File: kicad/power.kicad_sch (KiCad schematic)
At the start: 27 parts, among them J28 Eurorack Power Small, J29 Conn_01x04_Socket, J30 Conn_01x04_Header, U1 CD4093, U2 TL072, U3 TL072, U4 TL074, U5 LM13700, U6 LM13700, U7 LM13700

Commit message: Tweaking schematic and bom values
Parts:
- C21, C22: value 1uF -> 10uF
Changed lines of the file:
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@@
   (symbol (lib_id "Device:C_Polarized") (at 67.31 68.58 0) (unit 1)
     (in_bom yes) (on_board yes) (fields_autoplaced)
-    (property "Reference" "C22" (id 0) (at 70.231 66.7825 0)
-      (effects (font (size 1.27 1.27)) (justify left))
-    )
-    (property "Value" "1uF" (id 1) (at 70.231 69.5576 0)
+    (property "Reference" "C22" (id 0) (at 70.231 66.8563 0)
+      (effects (font (size 1.27 1.27)) (justify left))
+    )
+    (property "Value" "10uF" (id 1) (at 70.231 69.3932 0)
       (effects (font (size 1.27 1.27)) (justify left))
     )
@@
   (symbol (lib_id "Device:C_Polarized") (at 67.31 49.53 0) (unit 1)
     (in_bom yes) (on_board yes) (fields_autoplaced)
-    (property "Reference" "C21" (id 0) (at 70.231 47.7325 0)
-      (effects (font (size 1.27 1.27)) (justify left))
-    )
-    (property "Value" "1uF" (id 1) (at 70.231 50.5076 0)
-      (effects (font (size 1.27 1.27)) (justify left))
-    )
+    (property "Reference" "C21" (id 0) (at 70.231 47.8063 0)
+      (effects (font (size 1.27 1.27)) (justify left))
+    )
+    (property "Value" "10uF" (id 1) (at 70.231 50.3432 0)
+      (effects (font (size 1.27 1.27)) (justify left))
+    )

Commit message: Moving mixer opamp to front board
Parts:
- removed U3: TL072, rumblesan-standard-parts:DIP-8_W7.62mm_Socket, symbol Amplifier_Operational:TL072
- added U3: TL074, rumblesan-standard-parts:DIP-14_W7.62mm_Socket, symbol Amplifier_Operational:TL074
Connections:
- net +12V: now also U3.4 (V+)
- net -12V: now also U3.11 (V-)
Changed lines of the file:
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@@
     (pin "2")
   )
-  (symbol (lib_id "Amplifier_Operational:TL072") (at 111.76 46.99 0) (unit 3)
+  (symbol (lib_id "Amplifier_Operational:TL074") (at 111.76 46.99 0) (unit 5)
     (in_bom yes) (on_board yes) (fields_autoplaced)
-    (property "Reference" "U3" (id 0) (at 109.855 46.0815 0)
+    (property "Reference" "U3" (id 0) (at 109.855 46.1553 0)
       (effects (font (size 1.27 1.27)) (justify left))
     )
-    (property "Value" "TL072" (id 1) (at 109.855 48.8566 0)
+    (property "Value" "TL074" (id 1) (at 109.855 48.6922 0)
       (effects (font (size 1.27 1.27)) (justify left))
     )
-    (property "Footprint" "rumblesan-standard-parts:DIP-8_W7.62mm_Socket" (id 2) (at 111.76 46.99 0)
+    (property "Footprint" "rumblesan-standard-parts:DIP-14_W7.62mm_Socket" (id 2) (at 110.49 44.45 0)
       (effects (font (size 1.27 1.27)) hide)
     )
-    (property "Datasheet" "http://www.ti.com/lit/ds/symlink/tl071.pdf" (id 3) (at 111.76 46.99 0)
+    (property "Datasheet" "http://www.ti.com/lit/ds/symlink/tl071.pdf" (id 3) (at 113.03 41.91 0)
       (effects (font (size 1.27 1.27)) hide)
     )
@@
     (pin "6")
     (pin "7")
+    (pin "10")
+    (pin "8")
+    (pin "9")
+    (pin "12")
+    (pin "13")
+    (pin "14")
+    (pin "11")
     (pin "4")
-    (pin "8")
   )
   (symbol (lib_id "power:GND") (at 153.67 78.74 0) (unit 1)

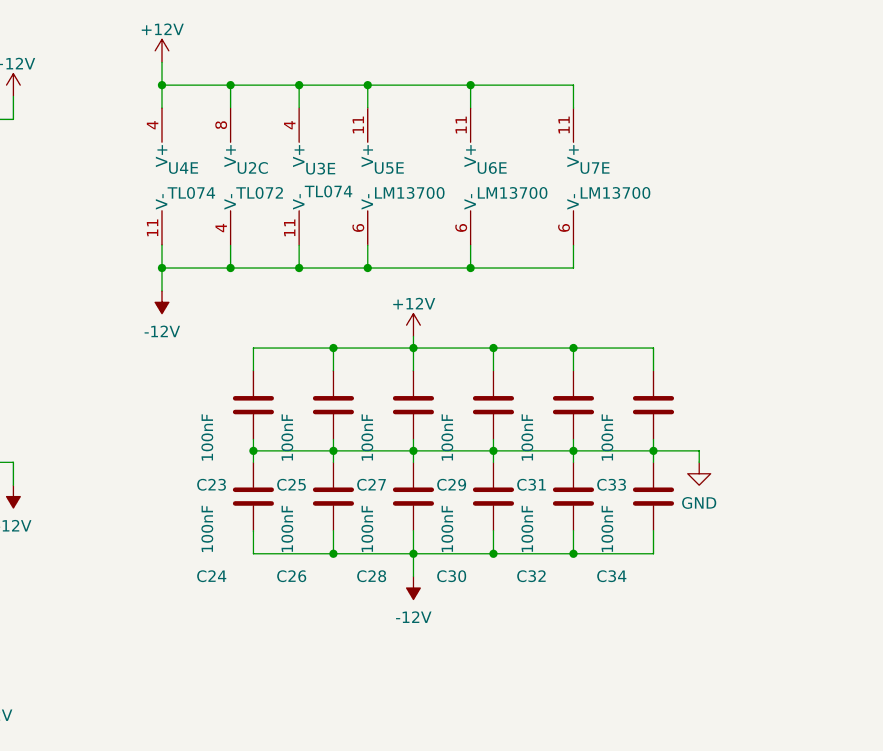
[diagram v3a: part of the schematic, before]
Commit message: slimlining opamp count and more moving around
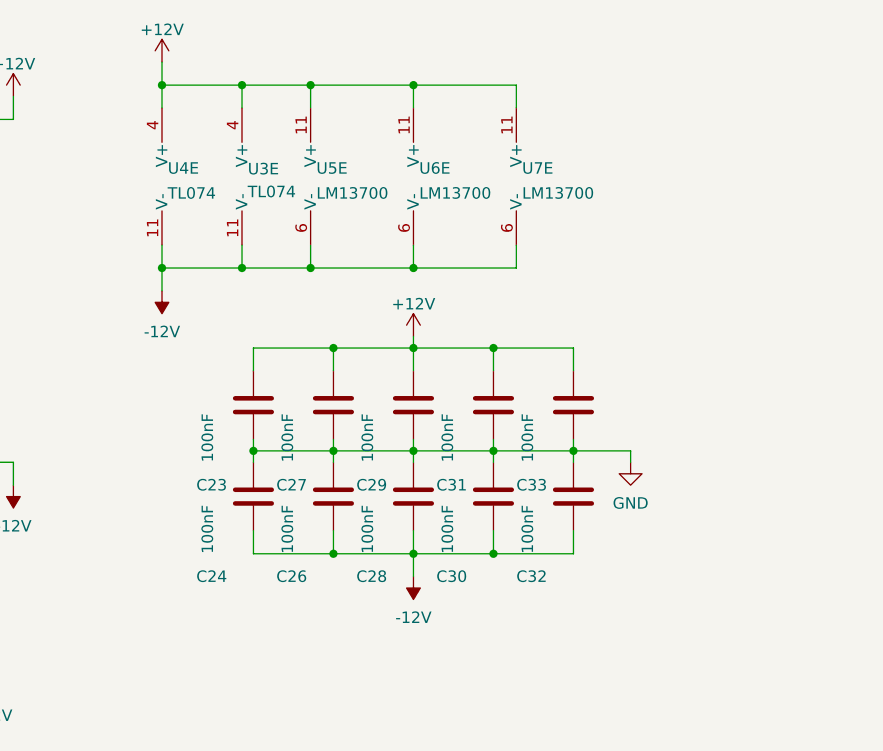
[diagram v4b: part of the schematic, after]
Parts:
- removed C25, C34: 100nF, rumblesan-standard-parts:C_Rect_L7.0mm_W3.5mm_P5.00mm, symbol Device:C
- removed U2: TL072, rumblesan-standard-parts:DIP-8_W7.62mm_Socket, symbol Amplifier_Operational:TL072
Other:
- moved on the sheet: C27, C29, C31, C33, U3E, U5E, U6E, U7E

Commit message: Final fixes and tweaks (hopefully)
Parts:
- added C25, C34: 100nF, rumblesan-standard-parts:C_Rect_L7.0mm_W3.5mm_P5.00mm, symbol Device:C
- added U2: TL072, rumblesan-standard-parts:DIP-8_W7.62mm_Socket, symbol Amplifier_Operational:TL072
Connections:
- net +12V: now also C25.1, U2.8 (V+)
- net -12V: now also C34.2, U2.4 (V-)
- net GND: now also C25.2, C34.1
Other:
- moved on the sheet: C32, C33, U3E, U4E, U5E, U6E, U7E

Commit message: geographically reannotate all the parts
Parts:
- renumbered C21 to C10, C34 to C13, C22 to C14, C23 to C22, C28 to C25, C29 to C26, C32 to C28, C33 to C31, C24 to C32, C26 to C34, C31 to C4, C30 to C5, C27 to C8, C25 to C9, D7 to D3, D8 to D4, J29 to J2, J28 to J3, J30 to J6, U3 to U1, U1 to U2, U2 to U3, U5 to U4, U4 to U5, U7 to U6, U6 to U7
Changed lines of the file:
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@@
   (symbol (lib_id "Device:C") (at 139.7 72.39 0) (unit 1)
     (in_bom yes) (on_board yes)
-    (property "Reference" "C25" (id 0) (at 133.35 81.28 0)
+    (property "Reference" "C9" (id 0) (at 133.35 81.28 0)
       (effects (font (size 1.27 1.27)) (justify left))
     )
@@
   (symbol (lib_id "Device:C_Polarized") (at 67.31 68.58 0) (unit 1)
     (in_bom yes) (on_board yes) (fields_autoplaced)
-    (property "Reference" "C22" (id 0) (at 70.231 66.8563 0)
+    (property "Reference" "C14" (id 0) (at 70.231 66.8563 0)
       (effects (font (size 1.27 1.27)) (justify left))
     )
@@
   (symbol (lib_id "Device:C") (at 139.7 82.55 0) (unit 1)
     (in_bom yes) (on_board yes)
-    (property "Reference" "C34" (id 0) (at 133.35 91.44 0)
+    (property "Reference" "C13" (id 0) (at 133.35 91.44 0)
       (effects (font (size 1.27 1.27)) (justify left))
     )
@@
   (symbol (lib_id "Device:C") (at 113.03 72.39 0) (unit 1)
     (in_bom yes) (on_board yes)
-    (property "Reference" "C27" (id 0) (at 106.68 81.28 0)
+    (property "Reference" "C8" (id 0) (at 106.68 81.28 0)
       (effects (font (size 1.27 1.27)) (justify left))
     )
@@
   (symbol (lib_id "Amplifier_Operational:TL074") (at 119.38 36.83 0) (unit 5)
     (in_bom yes) (on_board yes) (fields_autoplaced)
-    (property "Reference" "U3" (id 0) (at 117.475 35.9953 0)
+    (property "Reference" "U1" (id 0) (at 117.475 35.9953 0)
       (effects (font (size 1.27 1.27)) (justify left))
     )
@@
   (symbol (lib_id "Device:D") (at 60.96 78.74 0) (unit 1)
     (in_bom yes) (on_board yes) (fields_autoplaced)
-    (property "Reference" "D8" (id 0) (at 60.96 73.5035 0))
+    (property "Reference" "D4" (id 0) (at 60.96 73.5035 0))
     (property "Value" "1N5818" (id 1) (at 60.96 76.2786 0))
     (property "Footprint" "rumblesan-standard-parts:D_DO-41_SOD81_P10.16mm_Horizontal" (id 2) (at 60.96 78.74 0)
@@
   (symbol (lib_id "Eurorack_Hardware:Eurorack Power Small") (at 46.99 59.69 0) (unit 1)
     (in_bom yes) (on_board yes)
-    (property "Reference" "J28" (id 0) (at 47.625 50.0593 0))
+    (property "Reference" "J3" (id 0) (at 47.625 50.0593 0))
     (property "Value" "Eurorack Power Small" (id 1) (at 43.18 59.69 90))
     (property "Footprint" "eurorack-power:Eurorack_PowerHeader_2x05_P2.54mm_Shrouded" (id 2) (at 46.99 68.58 0)
@@
   (symbol (lib_id "Connector:Conn_01x04_Female") (at 62.23 114.3 0) (unit 1)
     (in_bom yes) (on_board yes)
-    (property "Reference" "J29" (id 0) (at 58.42 109.22 0)
+    (property "Reference" "J2" (id 0) (at 58.42 109.22 0)
       (effects (font (size 1.27 1.27)) (justify left))
     )
@@
   (symbol (lib_id "Amplifier_Operational:LM13700") (at 149.86 36.83 0) (unit 5)
     (in_bom yes) (on_board yes)
-    (property "Reference" "U7" (id 0) (at 147.955 35.9215 0)
+    (property "Reference" "U6" (id 0) (at 147.955 35.9215 0)
       (effects (font (size 1.27 1.27)) (justify left))
     )
@@
   (symbol (lib_id "Device:C") (at 148.59 82.55 0) (unit 1)
     (in_bom yes) (on_board yes)
-    (property "Reference" "C32" (id 0) (at 142.24 91.44 0)
+    (property "Reference" "C28" (id 0) (at 142.24 91.44 0)
       (effects (font (size 1.27 1.27)) (justify left))
     )
@@
   (symbol (lib_id "Device:C_Polarized") (at 67.31 49.53 0) (unit 1)
     (in_bom yes) (on_board yes) (fields_autoplaced)
-    (property "Reference" "C21" (id 0) (at 70.231 47.8063 0)
+    (property "Reference" "C10" (id 0) (at 70.231 47.8063 0)
       (effects (font (size 1.27 1.27)) (justify left))
     )
@@
   (symbol (lib_id "Amplifier_Operational:TL072") (at 101.6 36.83 0) (unit 3)
     (in_bom yes) (on_board yes) (fields_autoplaced)
-    (property "Reference" "U2" (id 0) (at 99.695 35.9953 0)
+    (property "Reference" "U3" (id 0) (at 99.695 35.9953 0)
       (effects (font (size 1.27 1.27)) (justify left))
     )
@@
   (symbol (lib_id "Device:D") (at 60.96 40.64 180) (unit 1)
     (in_bom yes) (on_board yes) (fields_autoplaced)
-    (property "Reference" "D7" (id 0) (at 60.96 35.4035 0))
+    (property "Reference" "D3" (id 0) (at 60.96 35.4035 0))
     (property "Value" "1N5818" (id 1) (at 60.96 38.1786 0))
     (property "Footprint" "rumblesan-standard-parts:D_DO-41_SOD81_P10.16mm_Horizontal" (id 2) (at 60.96 40.64 0)
@@
   (symbol (lib_id "Device:C") (at 113.03 82.55 0) (unit 1)
     (in_bom yes) (on_board yes)
-    (property "Reference" "C26" (id 0) (at 106.68 91.44 0)
+    (property "Reference" "C34" (id 0) (at 106.68 91.44 0)
       (effects (font (size 1.27 1.27)) (justify left))
     )
@@
   (symbol (lib_id "Device:C") (at 130.81 72.39 0) (unit 1)
     (in_bom yes) (on_board yes)
-    (property "Reference" "C31" (id 0) (at 124.46 81.28 0)
+    (property "Reference" "C4" (id 0) (at 124.46 81.28 0)
       (effects (font (size 1.27 1.27)) (justify left))
     )
@@
   (symbol (lib_id "4xxx:HEF4093B") (at 199.39 57.15 0) (unit 5)
     (in_bom yes) (on_board yes)
-    (property "Reference" "U1" (id 0) (at 205.232 56.2415 0)
+    (property "Reference" "U2" (id 0) (at 205.232 56.2415 0)
       (effects (font (size 1.27 1.27)) (justify left))
     )
@@
   (symbol (lib_id "Device:C") (at 121.92 72.39 0) (unit 1)
     (in_bom yes) (on_board yes)
-    (property "Reference" "C29" (id 0) (at 115.57 81.28 0)
+    (property "Reference" "C26" (id 0) (at 115.57 81.28 0)
       (effects (font (size 1.27 1.27)) (justify left))
     )
@@
   (symbol (lib_id "Amplifier_Operational:LM13700") (at 138.43 36.83 0) (unit 5)
     (in_bom yes) (on_board yes) (fields_autoplaced)
-    (property "Reference" "U6" (id 0) (at 136.525 35.9215 0)
+    (property "Reference" "U7" (id 0) (at 136.525 35.9215 0)
       (effects (font (size 1.27 1.27)) (justify left))
     )
@@
   (symbol (lib_id "Device:C") (at 121.92 82.55 0) (unit 1)
     (in_bom yes) (on_board yes)
-    (property "Reference" "C28" (id 0) (at 115.57 91.44 0)
+    (property "Reference" "C25" (id 0) (at 115.57 91.44 0)
       (effects (font (size 1.27 1.27)) (justify left))
     )
@@
   (symbol (lib_id "Device:C") (at 148.59 72.39 0) (unit 1)
     (in_bom yes) (on_board yes)
-    (property "Reference" "C33" (id 0) (at 142.24 81.28 0)
+    (property "Reference" "C31" (id 0) (at 142.24 81.28 0)
       (effects (font (size 1.27 1.27)) (justify left))
     )
@@
   (symbol (lib_id "Connector:Conn_01x04_Male") (at 68.58 114.3 0) (unit 1)
     (in_bom yes) (on_board yes)
-    (property "Reference" "J30" (id 0) (at 71.12 109.22 0))
+    (property "Reference" "J6" (id 0) (at 71.12 109.22 0))
     (property "Value" "Conn_01x04_Header" (id 1) (at 67.31 115.57 90)
       (effects (font (size 1.27 1.27)) hide)
@@
   (symbol (lib_id "Amplifier_Operational:TL074") (at 110.49 36.83 0) (unit 5)
     (in_bom yes) (on_board yes) (fields_autoplaced)
-    (property "Reference" "U4" (id 0) (at 108.585 35.9215 0)
+    (property "Reference" "U5" (id 0) (at 108.585 35.9215 0)
       (effects (font (size 1.27 1.27)) (justify left))
     )
@@
   (symbol (lib_id "Device:C") (at 104.14 72.39 0) (unit 1)
     (in_bom yes) (on_board yes)
-    (property "Reference" "C23" (id 0) (at 97.79 81.28 0)
+    (property "Reference" "C22" (id 0) (at 97.79 81.28 0)
       (effects (font (size 1.27 1.27)) (justify left))
     )
@@
   (symbol (lib_id "Device:C") (at 104.14 82.55 0) (unit 1)
     (in_bom yes) (on_board yes)
-    (property "Reference" "C24" (id 0) (at 97.79 91.44 0)
+    (property "Reference" "C32" (id 0) (at 97.79 91.44 0)
       (effects (font (size 1.27 1.27)) (justify left))
     )
@@
   (symbol (lib_id "Amplifier_Operational:LM13700") (at 127 36.83 0) (unit 5)
     (in_bom yes) (on_board yes) (fields_autoplaced)
-    (property "Reference" "U5" (id 0) (at 125.095 35.9215 0)
+    (property "Reference" "U4" (id 0) (at 125.095 35.9215 0)
       (effects (font (size 1.27 1.27)) (justify left))
     )
@@
   (symbol (lib_id "Device:C") (at 130.81 82.55 0) (unit 1)
     (in_bom yes) (on_board yes)
-    (property "Reference" "C30" (id 0) (at 124.46 91.44 0)
-      (effects (font (size 1.27 1.27)) (justify left))
-    )
+    (property "Reference" "C5" (id 0) (at 124.46 91.44 0)
+      (effects (font (size 1.27 1.27)) (justify left))
+    )
